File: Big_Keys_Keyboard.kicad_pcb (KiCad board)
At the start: 2 copper layers, 100 x 134.5 mm, 9 parts, among them U1 MX1A-11NN, U2 MX1A-11NN, U3 MX1A-11NN, U4 MX1A-11NN

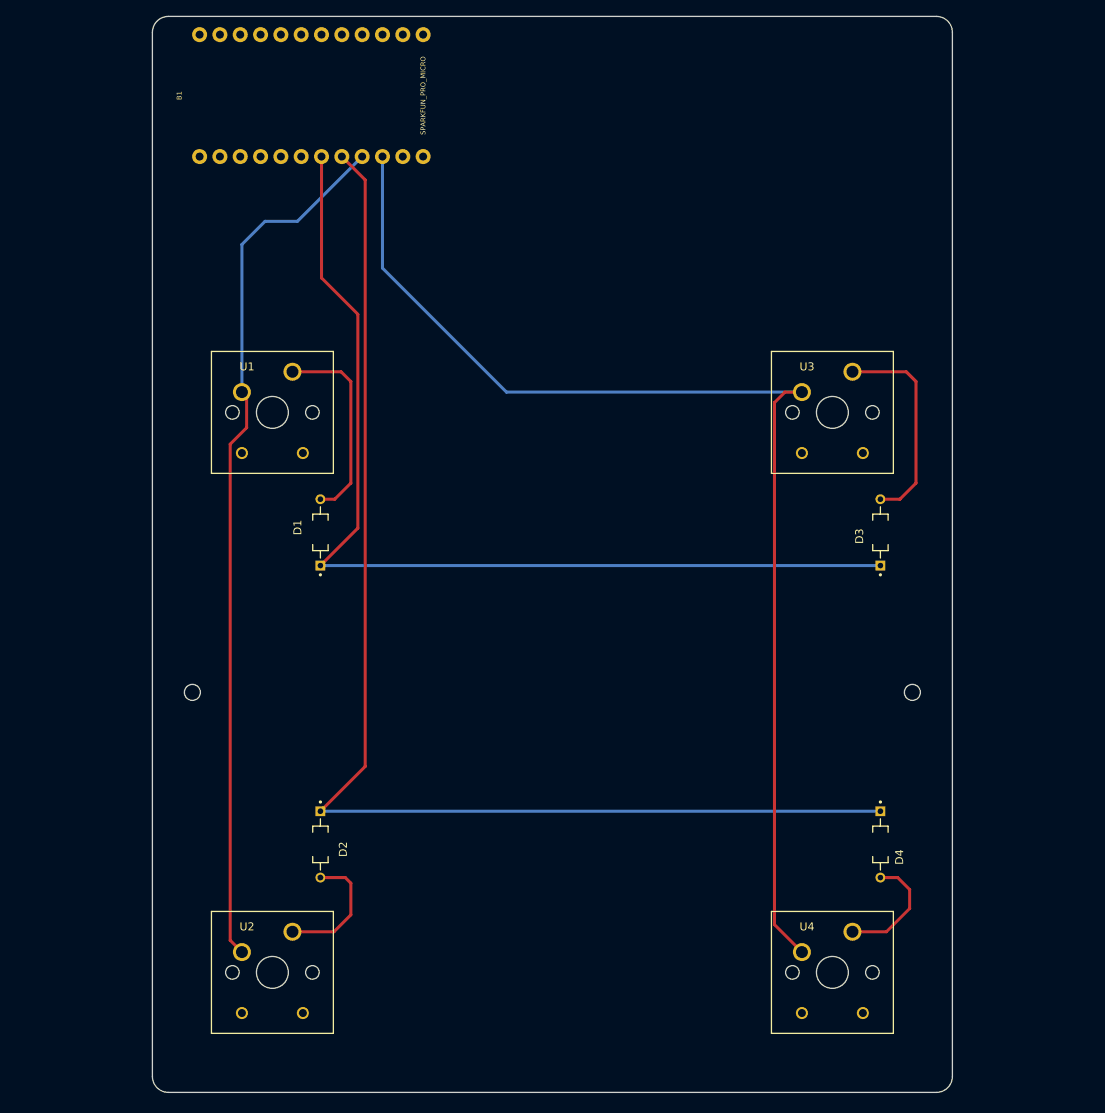
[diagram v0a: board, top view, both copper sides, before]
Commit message: i2c bus with jst 4 pin ports on each side connected
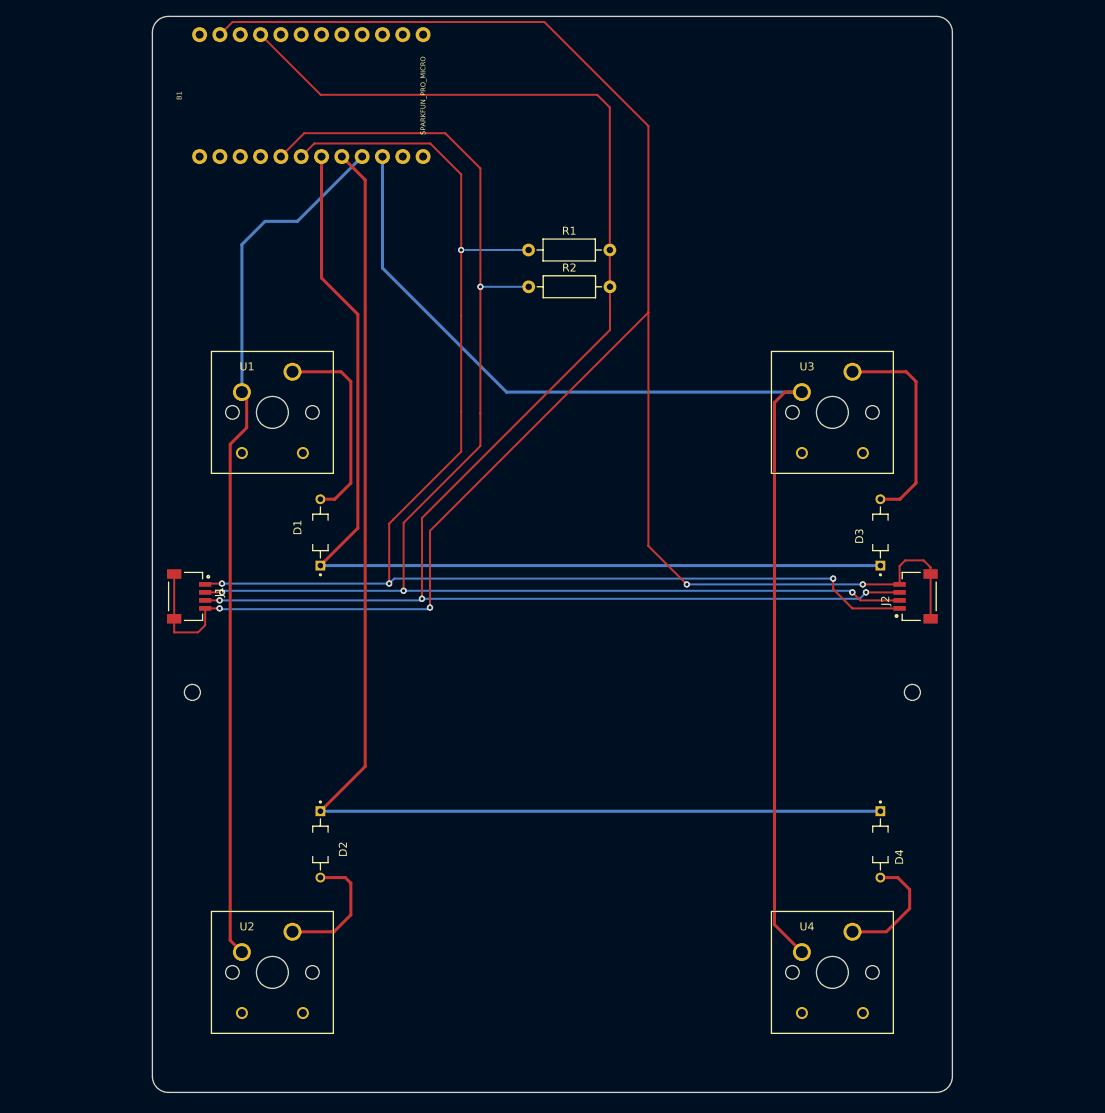
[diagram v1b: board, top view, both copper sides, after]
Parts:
- added J1: SM04B-SRSS-TB(LF)(SN), SM04B-SRSS-TB_LF__SN:JST_SM04B-SRSS-TB(LF)(SN), F.Cu at (82.6, 111.0)
- added J2: SM04B-SRSS-TB(LF)(SN), SM04B-SRSS-TB_LF__SN:JST_SM04B-SRSS-TB(LF)(SN), F.Cu at (169.4, 111.0)
- added R1: 10k, Resistor_THT:R_Axial_DIN0207_L6.3mm_D2.5mm_P10.16mm_Horizontal, F.Cu at (123.0, 67.7)
- added R2: 10k, Resistor_THT:R_Axial_DIN0207_L6.3mm_D2.5mm_P10.16mm_Horizontal, F.Cu at (123.0, 72.3)
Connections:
- B1 pad 21: unconnected-(B1-Pad21) -> VCC
- B1 pad 23: unconnected-(B1-Pad23) -> GND
- B1 pad 5: unconnected-(B1-Pad5) -> SDA
- B1 pad 6: unconnected-(B1-Pad6) -> SCL
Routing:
- net GND: track 0.00 -> 248.9 mm, vias 0 -> 4
- net VCC: track 0.00 -> 205.8 mm, vias 0 -> 3
- net SDA: track 0.00 -> 178.2 mm, vias 0 -> 4
- net SCL: track 0.00 -> 175.0 mm, vias 0 -> 4

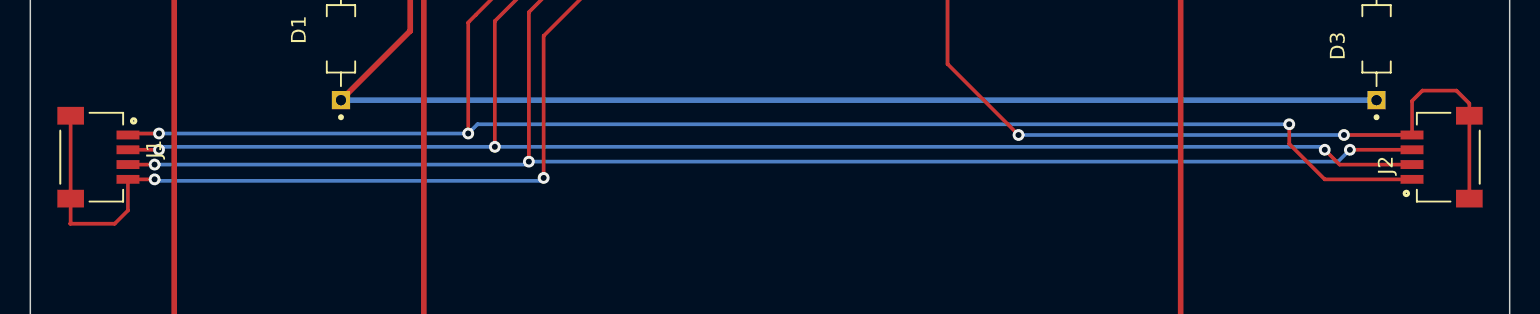
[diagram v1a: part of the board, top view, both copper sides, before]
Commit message: surface around i2c ports filled with f. cu connected to GND net
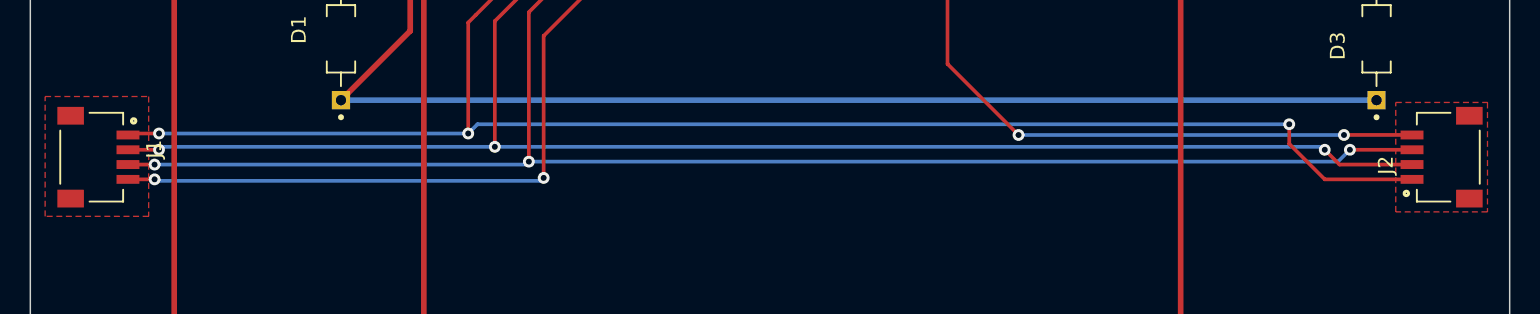
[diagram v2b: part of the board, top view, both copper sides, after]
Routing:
- net GND: track 248.9 -> 221.9 mm
- added copper zone on F.Cu, net GND
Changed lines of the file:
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@@
       (net 8 "ROW2") (pintype "passive"))
   )
-  (gr_line (start 174 173) (end 174 105.8) (layer "Dwgs.User") (width 0.15))
-  (gr_line (start 78 105.8) (end 174 105.8) (layer "Dwgs.User") (width 0.15))
-  (gr_line (start 78 173) (end 78 105.8) (layer "Dwgs.User") (width 0.15))
   (gr_line (start 176 40.5) (end 176 171) (layer "Edge.Cuts") (width 0.1))
   (gr_line (start 174 173) (end 78 173) (layer "Edge.Cuts") (width 0.1))
@@
   (segment (start 109.7 111.3) (end 164.4 111.3) (width 0.25) (layer "B.Cu") (net 21))
   (segment (start 109.7 111.3) (end 109.5 111.5) (width 0.25) (layer "B.Cu") (net 21))
-  (segment (start 173.275 108.2) (end 173.275 113.8) (width 0.25) (layer "F.Cu") (net 23))
-  (segment (start 170.1 106.5) (end 172.4 106.5) (width 0.25) (layer "F.Cu") (net 23))
-  (segment (start 78.7 115.5) (end 78.725 115.475) (width 0.25) (layer "F.Cu") (net 23))
   (segment (start 110.7 112.4) (end 110.7 102.8) (width 0.25) (layer "F.Cu") (net 23))
-  (segment (start 172.4 106.5) (end 173.275 107.375) (width 0.25) (layer "F.Cu") (net 23))
-  (segment (start 169.4 109.5) (end 169.4 107.2) (width 0.25) (layer "F.Cu") (net 23))
   (segment (start 86.02 39.2) (end 112.6 39.2) (width 0.25) (layer "F.Cu") (net 23))
   (segment (start 112.6 39.2) (end 125 39.2) (width 0.25) (layer "F.Cu") (net 23))
-  (segment (start 173.275 107.375) (end 173.275 108.2) (width 0.25) (layer "F.Cu") (net 23))
-  (segment (start 169.4 107.2) (end 170.1 106.5) (width 0.25) (layer "F.Cu") (net 23))
-  (segment (start 82.6 114.6) (end 81.7 115.5) (width 0.25) (layer "F.Cu") (net 23))
   (segment (start 84.44 40.78) (end 86.02 39.2) (width 0.25) (layer "F.Cu") (net 23))
-  (segment (start 81.7 115.5) (end 78.7 115.5) (width 0.25) (layer "F.Cu") (net 23))
   (segment (start 84.4 112.5) (end 82.6 112.5) (width 0.25) (layer "F.Cu") (net 23))
   (segment (start 164.8 109.5) (end 169.4 109.5) (width 0.25) (layer "F.Cu") (net 23))
-  (segment (start 78.725 113.8) (end 78.725 108.2) (width 0.25) (layer "F.Cu") (net 23))
   (segment (start 138 52.2) (end 138 75.5) (width 0.25) (layer "F.Cu") (net 23))
-  (segment (start 78.725 115.475) (end 78.725 113.8) (width 0.25) (layer "F.Cu") (net 23))
   (segment (start 110.7 102.8) (end 138 75.5) (width 0.25) (layer "F.Cu") (net 23))
-  (segment (start 82.6 112.5) (end 82.6 114.6) (width 0.25) (layer "F.Cu") (net 23))
   (segment (start 138 104.7) (end 142.8 109.5) (width 0.25) (layer "F.Cu") (net 23))
   (segment (start 138 75.5) (end 138 104.7) (width 0.25) (layer "F.Cu") (net 23))
@@
   (segment (start 170.65625 147.6375) (end 169.16475 146.146) (width 0.381) (layer "F.Cu") (net 28))
   (segment (start 163.51 152.92) (end 167.755 152.92) (width 0.381) (layer "F.Cu") (net 28))
+  (zone (net 23) (net_name "GND") (layer "F.Cu") (hatch edge 0.508)
+    (connect_pads (clearance 0.508))
+    (min_thickness 0.254) (filled_areas_thickness no)
+    (fill yes (thermal_gap 0.508) (thermal_bridge_width 0.508))
+    (polygon
+      (pts
+        (xy 84 115)
+        (xy 77 115)
+        (xy 77 106.9)
+        (xy 84 106.9)
+      )
+    )
+  )
+  (zone (net 23) (net_name "GND") (layer "F.Cu") (hatch edge 0.508)
+    (connect_pads (clearance 0.508))
+    (min_thickness 0.254) (filled_areas_thickness no)
+    (fill yes (thermal_gap 0.508) (thermal_bridge_width 0.508))
+    (polygon
+      (pts
+        (xy 174.5 114.7)
+        (xy 168.3 114.7)
+        (xy 168.3 107.3)
+        (xy 174.5 107.3)
+      )
+    )
+  )
 )

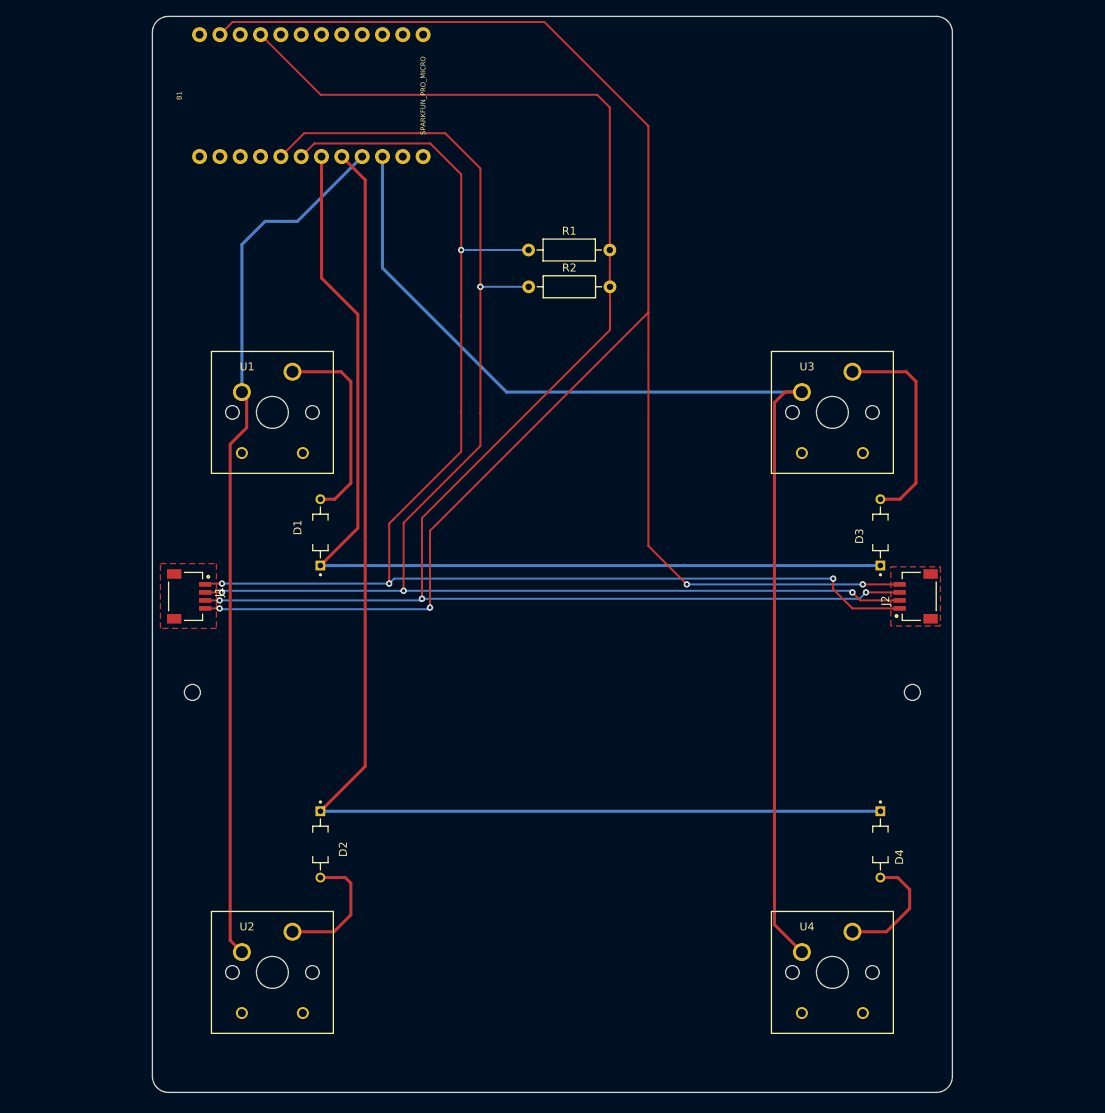
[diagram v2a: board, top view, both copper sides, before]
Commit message: PCB resized to fit the size of the keyboard
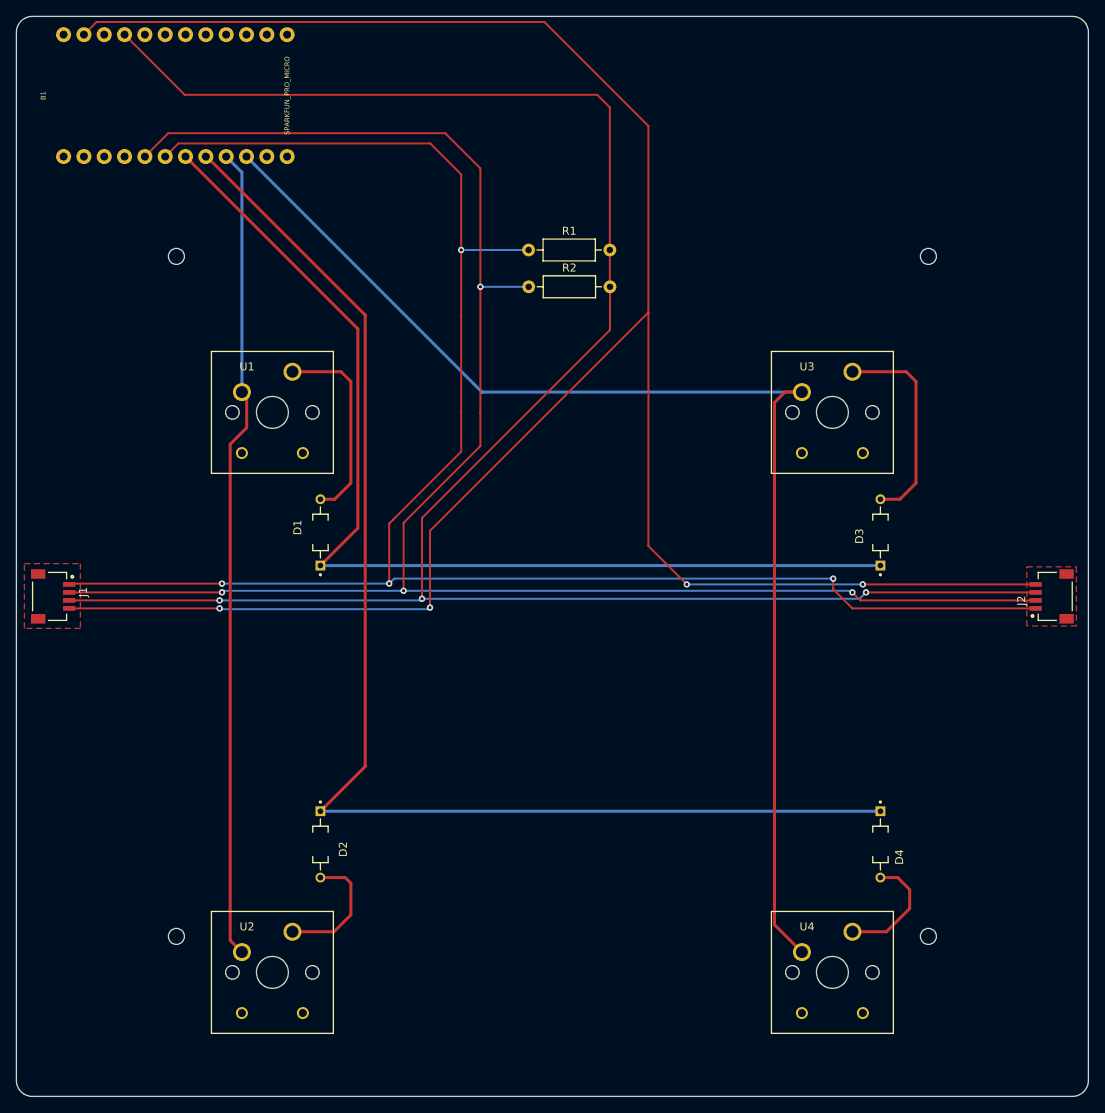
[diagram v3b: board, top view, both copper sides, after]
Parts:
- moved B1 17.0 mm to (77.6, 48.4)
- moved J1 17.0 mm to (65.6, 111.0)
- moved J2 17.0 mm to (186.4, 111.0)
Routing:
- net SCL: track 175.0 -> 226.0 mm
- net GND: track 221.9 -> 272.9 mm
- net VCC: track 205.8 -> 256.8 mm
- net SDA: track 178.2 -> 229.2 mm
- net COL2: track 146.9 -> 155.7 mm
- net COL1: track 109.7 -> 102.0 mm
- net ROW2: track 155.4 -> 162.5 mm
- net ROW1: track 124.9 -> 132.0 mm
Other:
- board size 100 x 134.5 mm -> 134 x 135 mm

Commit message: printable design ready
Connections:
- B1 pad 3: unconnected-(B1-Pad3) -> GND
- B1 pad 4: unconnected-(B1-Pad4) -> GND
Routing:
- added copper zone on B.Cu, net GND
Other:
- board text added: "Big-Keys-1.0"
